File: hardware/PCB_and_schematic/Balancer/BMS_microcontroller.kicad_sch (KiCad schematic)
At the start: 43 parts, among them J10 RS485, J8 ICP, J9 Conn_01x03, Q17 BC817, Q18 BC817, Q19 BC817, Q20 BC817, U4 PIC16F886-IP, U5 TL431LP, U6 ST485, U7 INA226

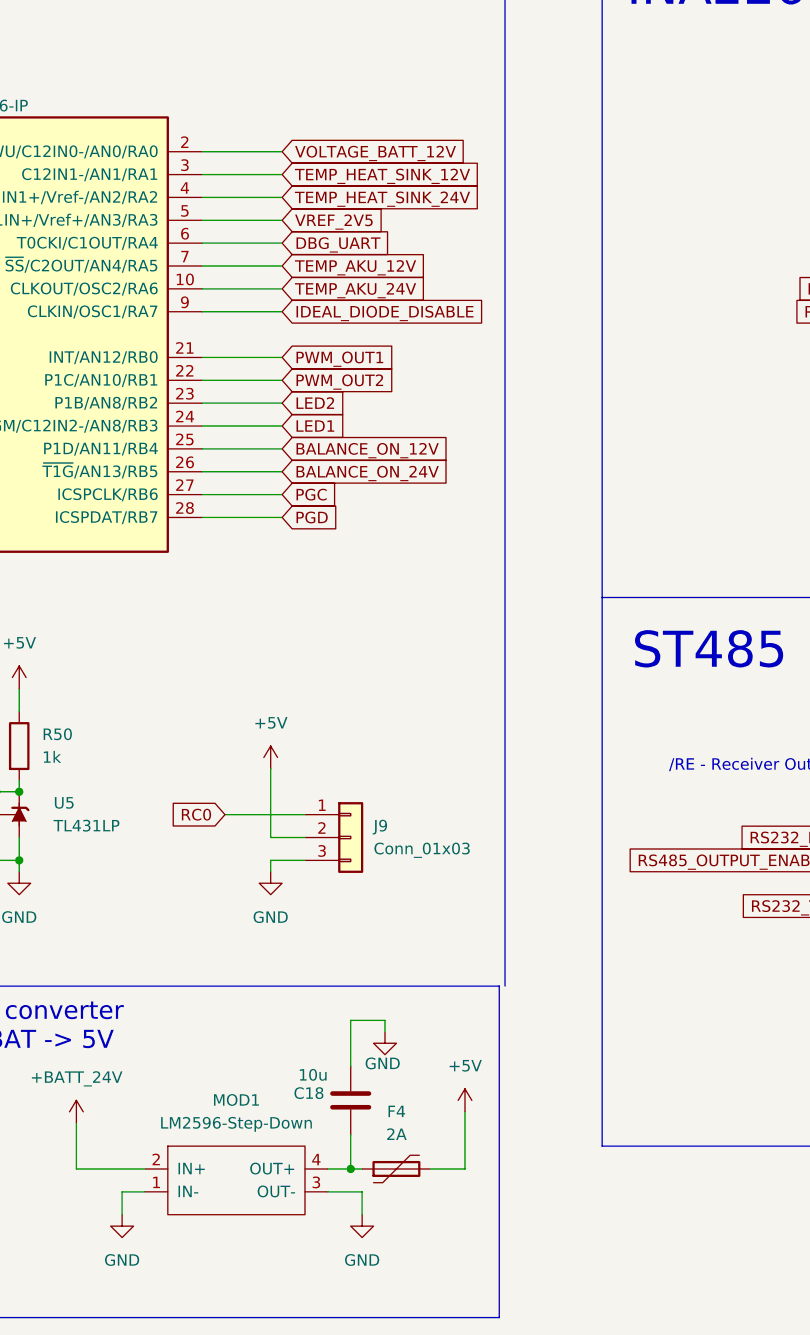
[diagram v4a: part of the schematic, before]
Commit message: balancer pcb progress
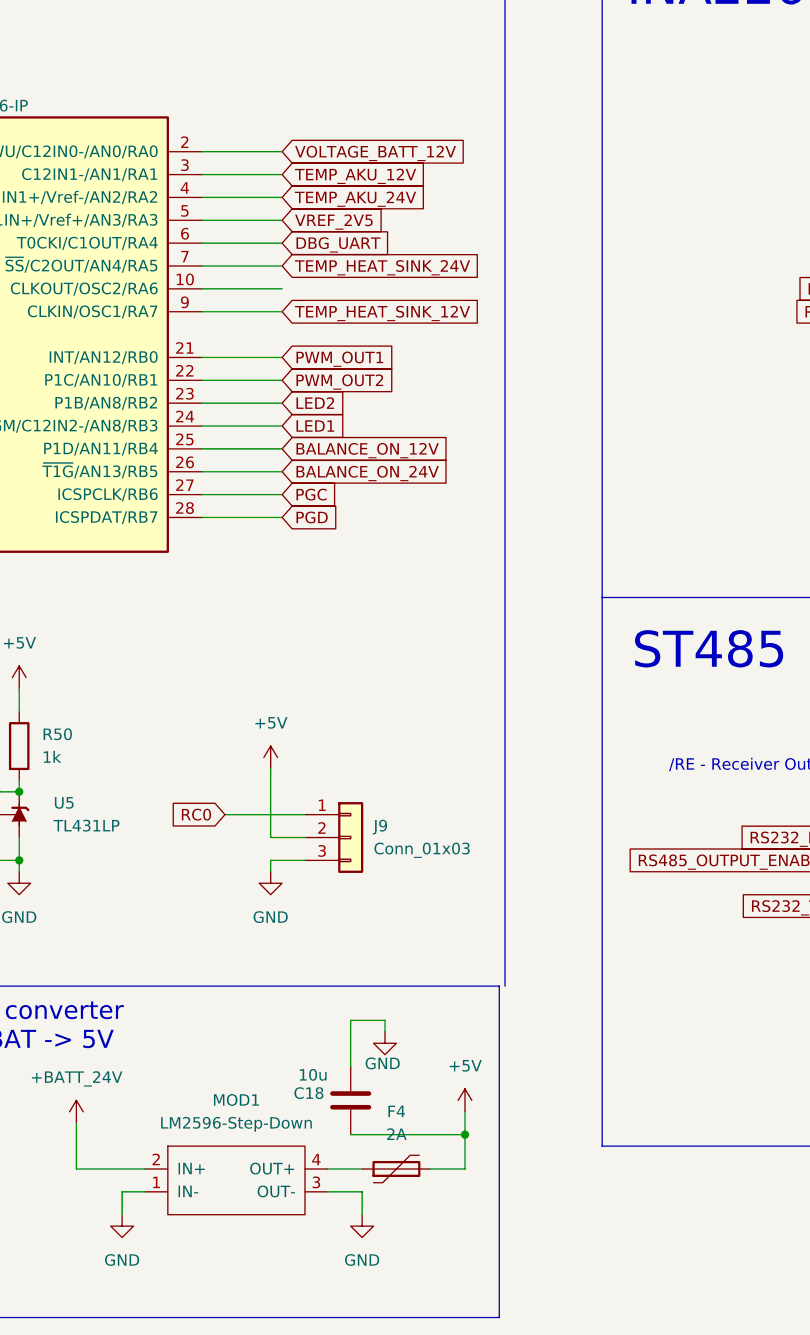
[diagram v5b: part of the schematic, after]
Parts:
- C18: footprint Capacitor_THT:CP_Radial_D6.3mm_P2.50mm -> Capacitor_Tantalum_SMD:CP_EIA-7343-31_Kemet-D
- D16, D17: footprint Diode_SMD:D_SMC -> Diode_SMD:D_SMA
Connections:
- net IDEAL_DIODE_DISABLE is gone; now on net TEMP_HEAT_SINK_12V: U4.9 (CLKIN/OSC1/RA7)
- net +5V: now also C18.2
- net TEMP_AKU_12V: now also U4.3 (C12IN1-/AN1/RA1); no longer U4.7 (~{SS}/C2OUT/AN4/RA5)
- net TEMP_AKU_24V: now also U4.4 (CVref/C2IN1+/Vref-/AN2/RA2); no longer U4.10 (CLKOUT/OSC2/RA6)
- net TEMP_HEAT_SINK_12V: no longer U4.3 (C12IN1-/AN1/RA1)
- net TEMP_HEAT_SINK_24V: now also U4.7 (~{SS}/C2OUT/AN4/RA5); no longer U4.4 (CVref/C2IN1+/Vref-/AN2/RA2)
- net at F4.1, MOD1.4 (OUT+): no longer C18.2
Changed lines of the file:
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@@
 	)
 	(junction
+		(at 156.21 161.29)
+		(diameter 0)
+		(color 0 0 0 0)
+	)
+	(junction
 		(at 248.92 46.99)
 		(diameter 0)
@@
 	)
 	(junction
-		(at 143.51 165.1)
-		(diameter 0)
-		(color 0 0 0 0)
-	)
-	(junction
 		(at 248.92 64.77)
 		(diameter 0)
@@
 	(wire
 		(pts
-			(xy 156.21 165.1) (xy 156.21 158.75)
+			(xy 156.21 165.1) (xy 156.21 161.29)
 		)
 		(stroke
@@
 		)
 	)
+	(wire
+		(pts
+			(xy 143.51 161.29) (xy 156.21 161.29)
+		)
+		(stroke
+			(width 0)
+			(type default)
+		)
+	)
 	(polyline
 		(pts
@@
 	(wire
 		(pts
+			(xy 156.21 161.29) (xy 156.21 158.75)
+		)
+		(stroke
+			(width 0)
+			(type default)
+		)
+	)
+	(wire
+		(pts
 			(xy 106.68 111.76) (xy 106.68 114.3)
 		)
@@
 		)
 	)
-	(wire
-		(pts
-			(xy 143.51 161.29) (xy 143.51 165.1)
-		)
-		(stroke
-			(width 0)
-			(type default)
-		)
-	)
 	(polyline
 		(pts
@@
 	(wire
 		(pts
-			(xy 140.97 165.1) (xy 143.51 165.1)
+			(xy 140.97 165.1) (xy 144.78 165.1)
 		)
 		(stroke
@@
 	(wire
 		(pts
-			(xy 143.51 165.1) (xy 144.78 165.1)
-		)
-		(stroke
-			(width 0)
-			(type default)
-		)
-	)
-	(wire
-		(pts
 			(xy 234.95 147.32) (xy 234.95 149.86)
 		)
@@
 	(global_label "TEMP_AKU_12V"
 		(shape input)
-		(at 135.89 64.77 0)
+		(at 135.89 54.61 0)
 		(fields_autoplaced yes)
 		(effects
@@
 		)
 		(property "Intersheetrefs" "${INTERSHEET_REFS}"
-			(at 152.8451 64.77 0)
+			(at 152.8451 54.61 0)
 			(effects
 				(font
@@
 	(global_label "TEMP_AKU_24V"
 		(shape input)
-		(at 135.89 67.31 0)
+		(at 135.89 57.15 0)
 		(fields_autoplaced yes)
 		(effects
@@
 		)
 		(property "Intersheetrefs" "${INTERSHEET_REFS}"
-			(at 152.8451 67.31 0)
+			(at 152.8451 57.15 0)
 			(effects
 				(font
@@
 		)
 	)
-	(global_label "IDEAL_DIODE_DISABLE"
-		(shape input)
-		(at 135.89 69.85 0)
-		(fields_autoplaced yes)
-		(effects
-			(font
-				(size 1.27 1.27)
-			)
-			(justify left)
-		)
-		(property "Intersheetrefs" "${INTERSHEET_REFS}"
-			(at 159.1952 69.85 0)
-			(effects
-				(font
-					(size 1.27 1.27)
-				)
-				(justify left)
-				(hide yes)
-			)
-		)
-	)
 	(global_label "R_shunt_H"
 		(shape input)
@@
 	(global_label "TEMP_HEAT_SINK_12V"
 		(shape input)
-		(at 135.89 54.61 0)
+		(at 135.89 69.85 0)
 		(fields_autoplaced yes)
 		(effects
@@
 		)
 		(property "Intersheetrefs" "${INTERSHEET_REFS}"
-			(at 159.0741 54.61 0)
+			(at 159.0741 69.85 0)
 			(effects
 				(font
@@
 	(global_label "TEMP_HEAT_SINK_24V"
 		(shape input)
-		(at 135.89 57.15 0)
+		(at 135.89 64.77 0)
 		(fields_autoplaced yes)
 		(effects
@@
 		)
 		(property "Intersheetrefs" "${INTERSHEET_REFS}"
-			(at 159.0741 57.15 0)
+			(at 159.0741 64.77 0)
 			(effects
 				(font
@@
 			)
 		)
-		(property "Footprint" "Capacitor_THT:CP_Radial_D6.3mm_P2.50mm"
+		(property "Footprint" "Capacitor_Tantalum_SMD:CP_EIA-7343-31_Kemet-D"
 			(at 144.4752 161.29 0)
 			(effects
@@
 			)
 		)
-		(property "Footprint" "Diode_SMD:D_SMC"
+		(property "Footprint" "Diode_SMD:D_SMA"
 			(at 245.11 143.51 0)
 			(effects
@@
 			)
 		)
-		(property "Footprint" "Diode_SMD:D_SMC"
+		(property "Footprint" "Diode_SMD:D_SMA"
 			(at 240.03 143.51 0)
 			(effects

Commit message: Route balancer progress
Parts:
- removed J9: Conn_01x03, Connector_PinHeader_2.54mm:PinHeader_1x03_P2.54mm_Vertical, symbol Connector_Generic:Conn_01x03
- added J2: Conn_01x04, Connector_PinHeader_2.54mm:PinHeader_1x04_P2.54mm_Vertical, symbol Connector_Generic:Conn_01x04
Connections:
- net +5V: now also J2.3 (Pin_3)
- net GND: now also J2.4 (Pin_4)
- net RC0: now also J2.2 (Pin_2)
- net RA6: now reaches U4.10 (CLKOUT/OSC2/RA6)
- net RA6: now also J2.1 (Pin_1)
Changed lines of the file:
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@@
 	(wire
 		(pts
+			(xy 129.54 123.19) (xy 138.43 123.19)
+		)
+		(stroke
+			(width 0)
+			(type default)
+		)
+	)
+	(wire
+		(pts
 			(xy 234.95 135.89) (xy 234.95 139.7)
 		)
@@
 		)
 	)
+	(global_label "RA6"
+		(shape input)
+		(at 129.54 123.19 180)
+		(fields_autoplaced yes)
+		(effects
+			(font
+				(size 1.27 1.27)
+			)
+			(justify right)
+		)
+		(property "Intersheetrefs" "${INTERSHEET_REFS}"
+			(at 122.9867 123.19 0)
+			(effects
+				(font
+					(size 1.27 1.27)
+				)
+				(justify right)
+				(hide yes)
+			)
+		)
+	)
 	(global_label "RS232_TX"
 		(shape input)
@@
 		)
 	)
+	(global_label "RA6"
+		(shape input)
+		(at 135.89 67.31 0)
+		(fields_autoplaced yes)
+		(effects
+			(font
+				(size 1.27 1.27)
+			)
+			(justify left)
+		)
+		(property "Intersheetrefs" "${INTERSHEET_REFS}"
+			(at 142.4433 67.31 0)
+			(effects
+				(font
+					(size 1.27 1.27)
+				)
+				(justify left)
+				(hide yes)
+			)
+		)
+	)
 	(global_label "VREF_2V5"
 		(shape input)
@@
 	)
 	(symbol
+		(lib_id "Connector_Generic:Conn_01x04")
+		(at 143.51 125.73 0)
+		(unit 1)
+		(exclude_from_sim no)
+		(in_bom yes)
+		(on_board yes)
+		(dnp no)
+		(fields_autoplaced yes)
+		(property "Reference" "J2"
+			(at 146.05 125.7299 0)
+			(effects
+				(font
+					(size 1.27 1.27)
+				)
+				(justify left)
+			)
+		)
+		(property "Value" "Conn_01x04"
+			(at 146.05 128.2699 0)
+			(effects
+				(font
+					(size 1.27 1.27)
+				)
+				(justify left)
+			)
+		)
+		(property "Footprint" "Connector_PinHeader_2.54mm:PinHeader_1x04_P2.54mm_Vertical"
+			(at 143.51 125.73 0)
+			(effects
+				(font
+					(size 1.27 1.27)
+				)
+				(hide yes)
+			)
+		)
+		(property "Datasheet" "~"
+			(at 143.51 125.73 0)
+			(effects
+				(font
+					(size 1.27 1.27)
+				)
+				(hide yes)
+			)
+		)
+		(property "Description" "Generic connector, single row, 01x04, script generated (kicad-library-utils/schlib/autogen/connector/)"
+			(at 143.51 125.73 0)
+			(effects
+				(font
+					(size 1.27 1.27)
+				)
+				(hide yes)
+			)
+		)
+		(pin "3"
+		)
+		(pin "2"
+		)
+		(pin "4"
+		)
+		(pin "1"
+		)
+		(instances
+			(project "Balancer"
+				(path "/555ba40f-9abb-4b99-82c6-07e888fda9fd/3b90ff07-e5cb-404b-939d-de320e975ba1"
+					(reference "J2")
+					(unit 1)
+				)
+			)
+		)
+	)
+	(symbol
 		(lib_id "power:+5V")
 		(at 156.21 158.75 0)
@@
 					(unit 1)
 				)
-			)
-		)
-	)
-	(symbol
-		(lib_id "Connector_Generic:Conn_01x03")
-		(at 143.51 128.27 0)
-		(unit 1)
-		(exclude_from_sim no)
-		(in_bom yes)
-		(on_board yes)
-		(dnp no)
-		(fields_autoplaced yes)
-		(property "Reference" "J9"
-			(at 146.05 126.9999 0)
-			(effects
-				(font
-					(size 1.27 1.27)
-				)
-				(justify left)
-			)
-		)
-		(property "Value" "Conn_01x03"
-			(at 146.05 129.5399 0)
-			(effects
-				(font
-					(size 1.27 1.27)
-				)
-				(justify left)
-			)
-		)
-		(property "Footprint" "Connector_PinHeader_2.54mm:PinHeader_1x03_P2.54mm_Vertical"
-			(at 143.51 128.27 0)
-			(effects
-				(font
-					(size 1.27 1.27)
-				)
-				(hide yes)
-			)
-		)
-		(property "Datasheet" "~"
-			(at 143.51 128.27 0)
-			(effects
-				(font
-					(size 1.27 1.27)
-				)
-				(hide yes)
-			)
-		)
-		(property "Description" "Generic connector, single row, 01x03, script generated (kicad-library-utils/schlib/autogen/connector/)"
-			(at 143.51 128.27 0)
-			(effects
-				(font
-					(size 1.27 1.27)
-				)
-				(hide yes)
-			)
-		)
-		(pin "3"
-		)
-		(pin "1"
-		)
-		(pin "2"
-		)
-		(instances
-			(project "Balancer"
-				(path "/555ba40f-9abb-4b99-82c6-07e888fda9fd/3b90ff07-e5cb-404b-939d-de320e975ba1"
-					(reference "J9")
-					(unit 1)
-				)

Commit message: pcb update
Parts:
- added D23, D5: LED, LED_SMD:LED_0805_2012Metric, symbol Device:LED
- added Q21, Q22: BC817, Package_TO_SOT_SMD:SOT-23, symbol Transistor_BJT:BC817
- added R77, R79: 10K, Resistor_SMD:R_0805_2012Metric_Pad1.20x1.40mm_HandSolder, symbol Device:R
- added R78, R80: 220R, Resistor_SMD:R_0805_2012Metric_Pad1.20x1.40mm_HandSolder, symbol Device:R
- MOD1: footprint My-Footprints-converters-modules:MP1584_Mini_3A_Step_Down_Conv -> My-Footprints-converters-modules:LM2596-Step-Down-Conv
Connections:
- net +5V: now also D23.1 (K), D5.1 (K)
- net GND: now also Q21.2 (E), Q22.2 (E)
- net RA6: now also R77.2
- net RC0: now also R79.2
- new net: Q22.3 (C), R80.1
- new net: D23.2 (A), R80.2
- new net: Q21.1 (B), R77.1
- new net: Q21.3 (C), R78.1
- new net: Q22.1 (B), R79.1
- new net: D5.2 (A), R78.2

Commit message: PCB footprint changes
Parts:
- C18: value 10u -> 100u/6,3V; footprint Capacitor_Tantalum_SMD:CP_EIA-7343-31_Kemet-D -> Capacitor_Tantalum_SMD:CP_EIA-3528-21_Kemet-B
- D23, D5: footprint LED_SMD:LED_0805_2012Metric -> LED_SMD:LED_PLCC-2_3.4x3.0mm_KA
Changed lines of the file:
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@@
 			)
 		)
-		(property "Value" "10u"
-			(at 137.668 154.686 0)
+		(property "Value" "100u/6,3V"
+			(at 132.334 154.686 0)
 			(effects
 				(font
@@
 			)
 		)
-		(property "Footprint" "Capacitor_Tantalum_SMD:CP_EIA-7343-31_Kemet-D"
+		(property "Footprint" "Capacitor_Tantalum_SMD:CP_EIA-3528-21_Kemet-B"
 			(at 144.4752 161.29 0)
 			(effects
@@
 			)
 		)
-		(property "Description" "Unpolarized capacitor"
+		(property "Description" "VISHAY TMCU SMD CODE JA8"
 			(at 143.51 157.48 0)
 			(effects
@@
 			)
 		)
-		(property "Footprint" "LED_SMD:LED_0805_2012Metric"
+		(property "Footprint" "LED_SMD:LED_PLCC-2_3.4x3.0mm_KA"
 			(at 327.66 121.92 0)
 			(effects
@@
 			)
 		)
-		(property "Footprint" "LED_SMD:LED_0805_2012Metric"
+		(property "Footprint" "LED_SMD:LED_PLCC-2_3.4x3.0mm_KA"
 			(at 311.15 121.92 0)
 			(effects
